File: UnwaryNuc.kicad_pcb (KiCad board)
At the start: 6 copper layers, 123.2 x 77.5 mm, 27 parts, among them Q1 2N3904, U1 NUC980DF71YC, U2 LAN8740A-EN-TR, U3 LAN8740A-EN-TR, U4 LD3985G18R_TSOT23, U5 LDK130-33_SOT23_SOT353

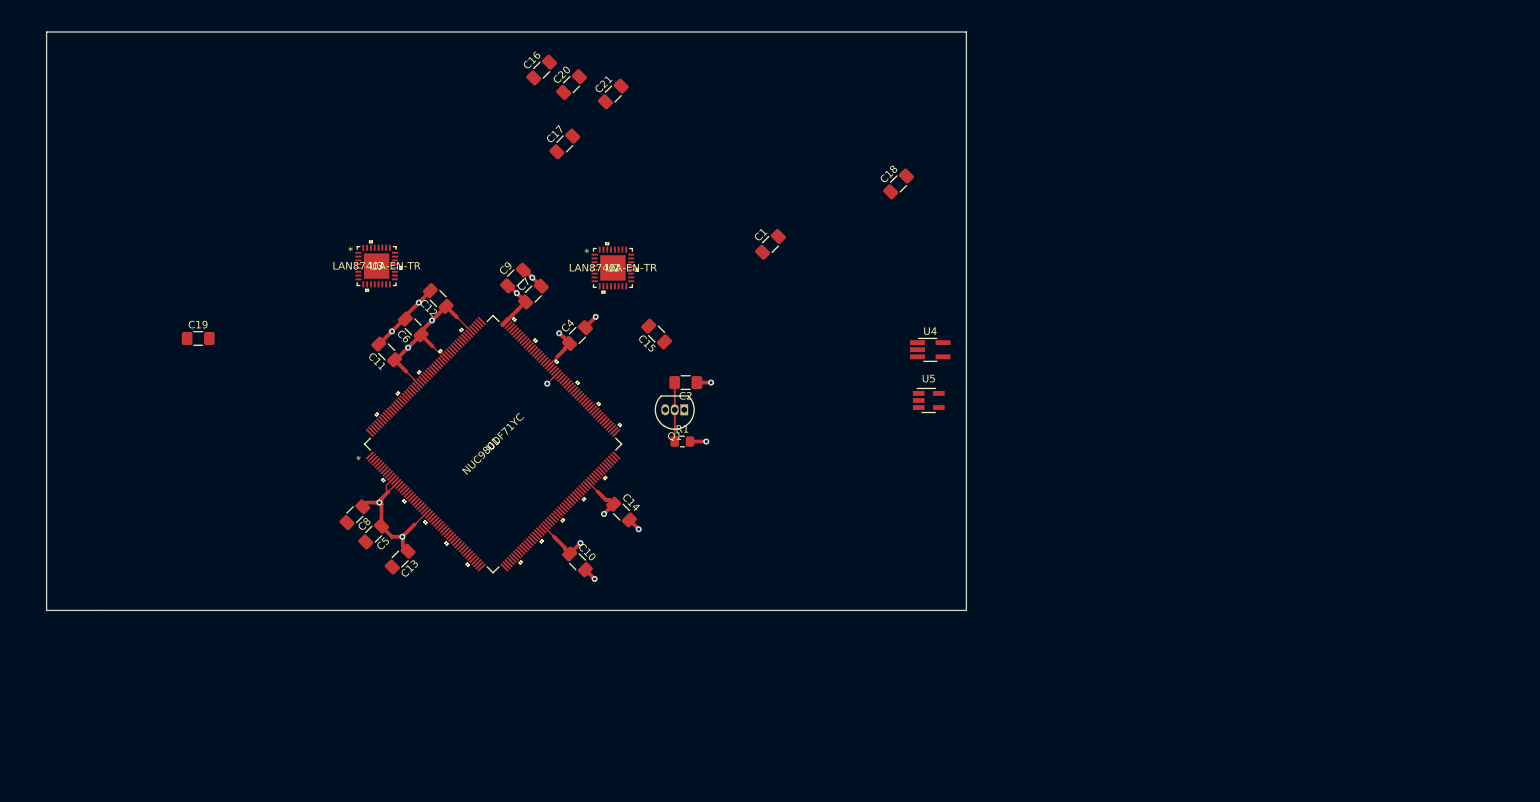
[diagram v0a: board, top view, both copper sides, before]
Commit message: added supply sequencing and stuff
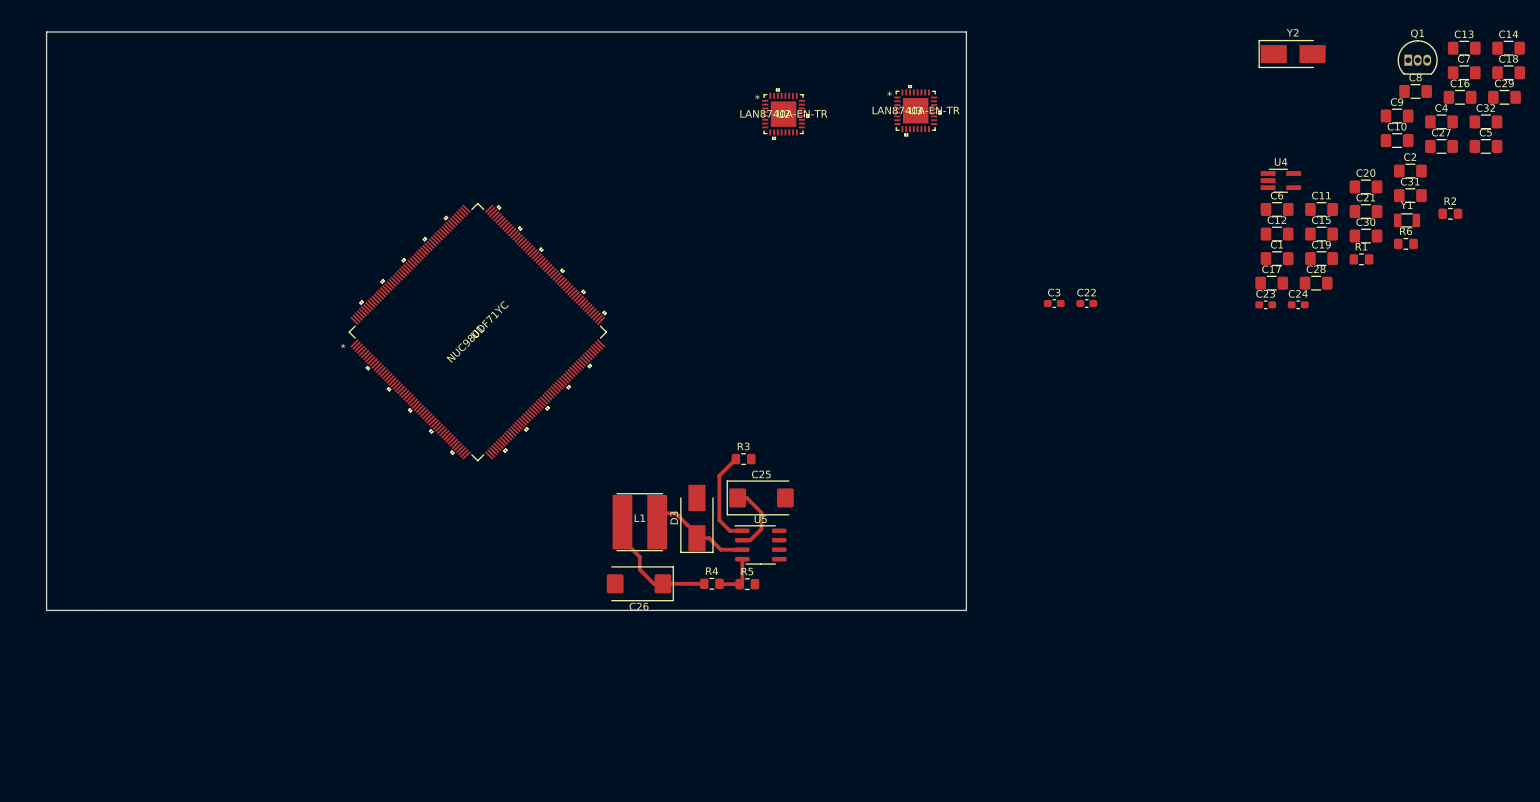
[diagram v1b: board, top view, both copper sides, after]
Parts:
- added C22: 8pf, Capacitor_SMD:C_0603_1608Metric_Pad1.05x0.95mm_HandSolder, F.Cu at (221.9, 87.2)
- added C23: 7pf, Capacitor_SMD:C_0603_1608Metric_Pad1.05x0.95mm_HandSolder, F.Cu at (245.8, 87.3)
- added C24: 7pf, Capacitor_SMD:C_0603_1608Metric_Pad1.05x0.95mm_HandSolder, F.Cu at (250.2, 87.3)
- added C25: T491D226k035AT, Capacitor_Tantalum_SMD:CP_EIA-7343-15_Kemet-W_Pad2.25x2.55mm_HandSolder, F.Cu at (178.3, 113.2)
- added C26: 293D127X96, Capacitor_Tantalum_SMD:CP_EIA-7343-43_Kemet-X_Pad2.25x2.55mm_HandSolder, F.Cu at (161.9, 124.7)
- added C27: 1u, Capacitor_SMD:C_1206_3216Metric_Pad1.42x1.75mm_HandSolder, F.Cu at (269.4, 66.1)
- added C28: 10n, Capacitor_SMD:C_1206_3216Metric_Pad1.42x1.75mm_HandSolder, F.Cu at (252.6, 84.4)
- added C29: 1u, Capacitor_SMD:C_1206_3216Metric_Pad1.42x1.75mm_HandSolder, F.Cu at (277.8, 59.5)
- added C3: 8pf, Capacitor_SMD:C_0603_1608Metric_Pad1.05x0.95mm_HandSolder, F.Cu at (217.5, 87.2)
- added C30: 1u, Capacitor_SMD:C_1206_3216Metric_Pad1.42x1.75mm_HandSolder, F.Cu at (259.2, 78.1)
- added C31: 1u, Capacitor_SMD:C_1206_3216Metric_Pad1.42x1.75mm_HandSolder, F.Cu at (265.2, 72.7)
- added C32: 1u, Capacitor_SMD:C_1206_3216Metric_Pad1.42x1.75mm_HandSolder, F.Cu at (275.3, 62.8)
- added D3: B240, 40V 2A, Diode_SMD:D_SMB_Handsoldering, F.Cu at (169.7, 115.9)
- added L1: CDRH6D38NP-150NC, UnwaryNuc:CDRH6D38_Sumida, F.Cu at (162.0, 116.5)
- added R2: 100k, Resistor_SMD:R_0805_2012Metric_Pad1.15x1.40mm_HandSolder, F.Cu at (270.6, 75.2)
- added R3: 100k, Resistor_SMD:R_0805_2012Metric_Pad1.15x1.40mm_HandSolder, F.Cu at (175.9, 108.0)
- added R4: 3.01k, Resistor_SMD:R_0805_2012Metric_Pad1.15x1.40mm_HandSolder, F.Cu at (171.7, 124.7)
- added R5: 1.78k, Resistor_SMD:R_0805_2012Metric_Pad1.15x1.40mm_HandSolder, F.Cu at (176.4, 124.8)
- added R6: 100k, Resistor_SMD:R_0805_2012Metric_Pad1.15x1.40mm_HandSolder, F.Cu at (264.6, 79.2)
- added Y1: ABS07-166, Crystal:Crystal_SMD_3215-2Pin_3.2x1.5mm, F.Cu at (264.8, 76.0)
- added Y2: NX5032GA, Crystal:Crystal_SMD_5032-2Pin_5.0x3.2mm_HandSoldering, F.Cu at (249.5, 53.8)
- U1: footprint footprints:NUC980DF71YC -> UnwaryNuc:NUC980DF71YC
- U4: value LD3985G18R_TSOT23 -> LD3985M18R_TSOT23
- U5: value LDK130-33_SOT23_SOT353 -> MIC4690; footprint Package_TO_SOT_SMD:SOT-23-5_HandSoldering -> Package_SO:SOIC-8_3.9x4.9mm_P1.27mm
- moved C13 158.1 mm to (272.4, 53.0), turned to 0 degrees
- moved C5 157.8 mm to (275.3, 66.1), turned to 0 degrees
- moved C8 153.0 mm to (265.9, 58.8), turned to 0 degrees
- moved C19 150.8 mm to (253.3, 81.2)
- moved C14 134.1 mm to (278.4, 53.0), turned to 0 degrees
- moved C7 128.1 mm to (272.4, 56.3), turned to 0 degrees
- moved C11 126.6 mm to (253.3, 74.6), turned to 0 degrees
- moved C10 123.4 mm to (263.4, 65.3), turned to 0 degrees
- moved C16 123.1 mm to (271.9, 59.5), turned to 0 degrees
- moved C9 120.0 mm to (263.4, 62.0), turned to 0 degrees
- moved C4 119.2 mm to (269.4, 62.8), turned to 0 degrees
- moved C6 116.8 mm to (247.3, 74.6), turned to 0 degrees
- moved C12 112.7 mm to (247.3, 77.9), turned to 0 degrees
- moved Q1 107.7 mm to (264.9, 54.6), turned to 0 degrees
- moved C20 107.3 mm to (259.2, 71.5), turned to 0 degrees
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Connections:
- U4 pad 2: Net-(U4-Pad2) -> GND
- U4 pad 5: Net-(U4-Pad5) -> +1V8
- U5 pad 5: Net-(U5-Pad5) -> GND
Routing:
- net +1V2: track 76.7 -> 0.00 mm, vias 9 -> 0
- net GND: track 21.1 -> 0.00 mm, vias 7 -> 0
- net /nRST: track 20.2 -> 0.00 mm, vias 1 -> 0
- net +3V3: track 0.00 -> 16.7 mm
- net Net-(R3-Pad1): track 0.00 -> 12.8 mm
- net Net-(D3-Pad1): track 0.00 -> 12.4 mm
- net Net-(C25-Pad1): track 0.00 -> 9.40 mm
- net Net-(C2-Pad2): track 7.91 -> 0.00 mm
- net Net-(R4-Pad2): track 0.00 -> 6.21 mm

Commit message: usb's connected, rmii nets assigned, some placement done
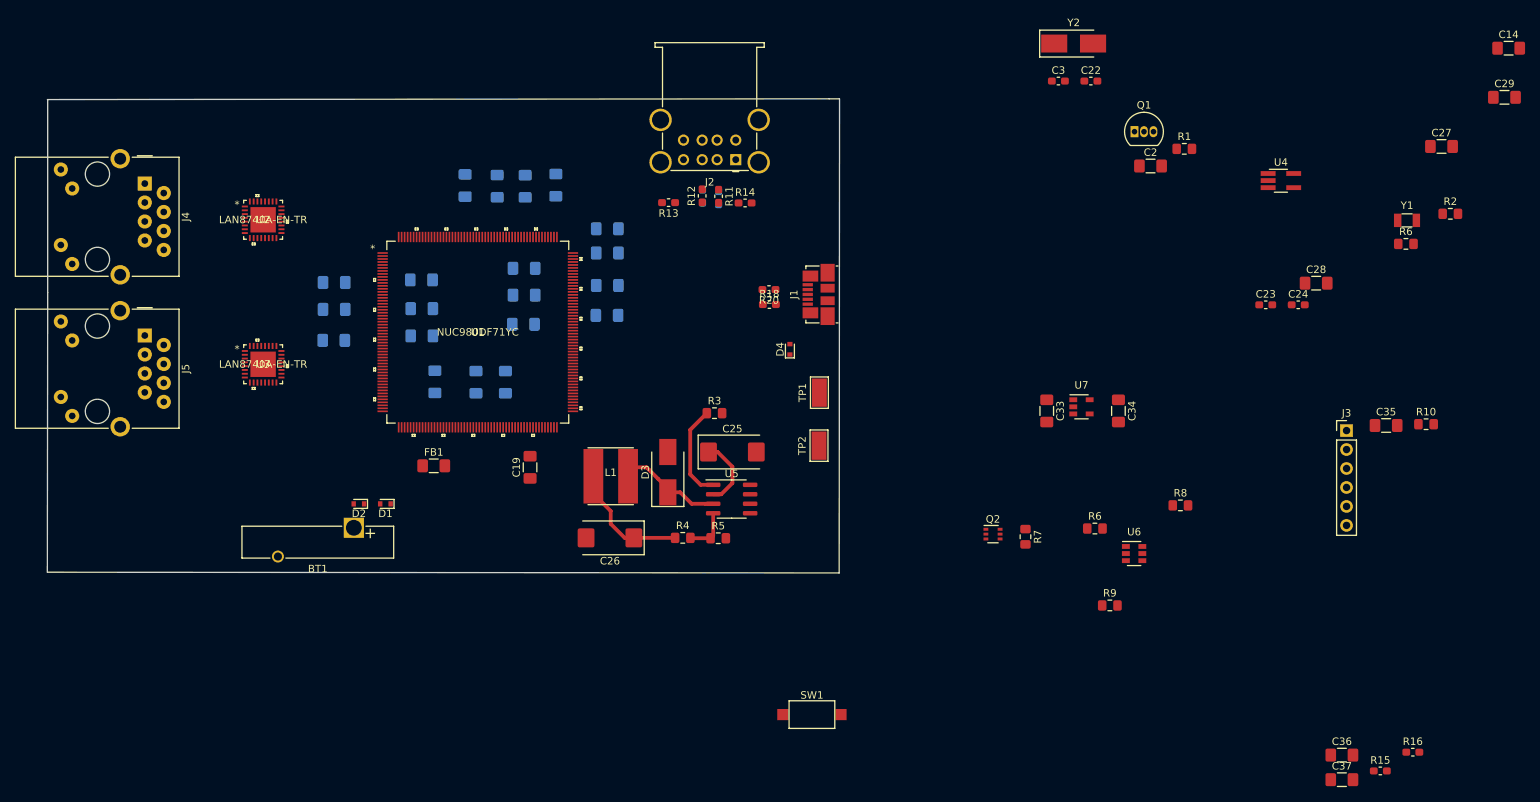
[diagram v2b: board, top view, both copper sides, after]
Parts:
- added BT1: Battery_Cell, Battery:Battery_Panasonic_CR2032-VS1N_Vertical_CircularHoles, F.Cu at (123.7, 117.2)
- added C33: 1u, Capacitor_SMD:C_1206_3216Metric_Pad1.42x1.75mm_HandSolder, F.Cu at (216.5, 101.5)
- added C34: 1u, Capacitor_SMD:C_1206_3216Metric_Pad1.42x1.75mm_HandSolder, F.Cu at (226.1, 101.5)
- added C35: 1u, Capacitor_SMD:C_1206_3216Metric_Pad1.42x1.75mm_HandSolder, F.Cu at (261.9, 103.5)
- added C36: 1u, Capacitor_SMD:C_1206_3216Metric_Pad1.42x1.75mm_HandSolder, F.Cu at (256.0, 147.6)
- added C37: 1u, Capacitor_SMD:C_1206_3216Metric_Pad1.42x1.75mm_HandSolder, F.Cu at (256.0, 150.9)
- added D1: D, Diode_SMD:D_SOD-523, F.Cu at (127.9, 114.0)
- added D2: D, Diode_SMD:D_SOD-523, F.Cu at (124.4, 114.0)
- added D4: D, Diode_SMD:D_SOD-523, F.Cu at (182.1, 93.3)
- added FB1: Ferrite_Bead_Small, Inductor_SMD:L_1206_3216Metric_Pad1.42x1.75mm_HandSolder, F.Cu at (134.4, 108.9)
- added J1: USB_B_Micro, Connector_USB:USB_Micro-B_Molex_47346-0001, F.Cu at (185.9, 86.0)
- added J2: USB_A_Dual, Connector_USB:USB_A_Wuerth_61400826021_Horizontal_Stacked, F.Cu at (174.8, 67.9)
- added J3: Conn_01x06_Male, Connector_PinHeader_2.54mm:PinHeader_1x06_P2.54mm_Vertical, F.Cu at (256.6, 104.2)
- added J4: RJ45_Amphenol_RJMG1BD3B8K1ANR, Connector_RJ:RJ45_Amphenol_RJMG1BD3B8K1ANR, F.Cu at (95.7, 71.1)
- added J5: RJ45_Amphenol_RJMG1BD3B8K1ANR, Connector_RJ:RJ45_Amphenol_RJMG1BD3B8K1ANR, F.Cu at (95.7, 91.5)
- added Q2: BC856BDW1, Package_TO_SOT_SMD:SOT-363_SC-70-6, F.Cu at (209.3, 118.0)
- added R10: 100k, Resistor_SMD:R_0805_2012Metric_Pad1.15x1.40mm_HandSolder, F.Cu at (267.3, 103.3)
- added R11: 27, Resistor_SMD:R_0603_1608Metric_Pad1.05x0.95mm_HandSolder, F.Cu at (172.6, 72.8)
- added R12: 27, Resistor_SMD:R_0603_1608Metric_Pad1.05x0.95mm_HandSolder, F.Cu at (170.3, 72.8)
- added R13: R, Resistor_SMD:R_0603_1608Metric_Pad1.05x0.95mm_HandSolder, F.Cu at (165.8, 73.7)
- added R14: R, Resistor_SMD:R_0603_1608Metric_Pad1.05x0.95mm_HandSolder, F.Cu at (176.1, 73.7)
- added R15: 12.1k, Resistor_SMD:R_0603_1608Metric_Pad1.05x0.95mm_HandSolder, F.Cu at (261.2, 149.8)
- added R16: 12.1k, Resistor_SMD:R_0603_1608Metric_Pad1.05x0.95mm_HandSolder, F.Cu at (265.5, 147.3)
- added R17: 4.7, Resistor_SMD:R_0603_1608Metric_Pad1.05x0.95mm_HandSolder, B.Cu at (170.4, 72.8)
- added R18: 4.7, Resistor_SMD:R_0603_1608Metric_Pad1.05x0.95mm_HandSolder, F.Cu at (179.3, 87.3)
- added R19: 4.7, Resistor_SMD:R_0603_1608Metric_Pad1.05x0.95mm_HandSolder, B.Cu at (172.6, 73.0)
- added R20: 4.7, Resistor_SMD:R_0603_1608Metric_Pad1.05x0.95mm_HandSolder, F.Cu at (179.3, 85.3)
- added R6: 100k, Resistor_SMD:R_0805_2012Metric_Pad1.15x1.40mm_HandSolder, F.Cu at (222.9, 117.3)
- added R7: 100k, Resistor_SMD:R_0805_2012Metric_Pad1.15x1.40mm_HandSolder, F.Cu at (213.7, 118.4)
- added R8: 100k, Resistor_SMD:R_0805_2012Metric_Pad1.15x1.40mm_HandSolder, F.Cu at (234.4, 114.2)
- added R9: 100k, Resistor_SMD:R_0805_2012Metric_Pad1.15x1.40mm_HandSolder, F.Cu at (224.9, 127.6)
- added SW1: SW_SPST, Button_Switch_SMD:SW_SPST_CK_RS282G05A3, F.Cu at (185.1, 142.2)
- added TP1: TestPoint, TestPoint:TestPoint_Keystone_5019_Minature, F.Cu at (186.1, 99.1)
- added TP2: TestPoint, TestPoint:TestPoint_Keystone_5019_Minature, F.Cu at (186.0, 106.2)
- added U6: LM3880, Package_TO_SOT_SMD:SOT-23-6, F.Cu at (228.2, 120.7)
- added U7: AP2127K-1.2, Package_TO_SOT_SMD:SOT-23-5, F.Cu at (221.2, 101.0)
- C1, C10, C11, C12, C13, C15, C16, C17, C18, C20, C21, C30, C31, C32, C4, C5, C6, C7, C8, C9: moved to B.Cu
- moved C8 148.7 mm to (121.0, 92.1), turned to 180 degrees
- moved C9 144.1 mm to (121.1, 84.3), turned to 180 degrees
- moved C5 138.9 mm to (140.1, 97.7), turned to 90 degrees
- moved C18 135.2 mm to (146.5, 86.0), turned to 180 degrees
- moved C11 132.9 mm to (121.1, 88.0), turned to 180 degrees
- moved C4 130.1 mm to (144.0, 97.7), turned to 90 degrees
- moved C20 128.0 mm to (132.8, 91.5)
- moved C16 127.4 mm to (146.5, 82.5), turned to 180 degrees
- moved C7 122.6 mm to (150.8, 71.3), turned to 90 degrees
- moved C15 120.9 mm to (132.8, 87.8)
- moved C32 120.5 mm to (157.6, 88.8)
- moved C13 119.1 mm to (157.7, 84.8)
- moved C10 116.9 mm to (146.7, 71.5), turned to 90 degrees
- moved C1 114.0 mm to (134.6, 97.7), turned to 90 degrees
- moved C17 113.9 mm to (132.8, 84.0)
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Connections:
- net Net-(C25-Pad1) renamed +5V
- net Net-(R3-Pad1) renamed /3V3EN
- net Net-(U1-Pad153) renamed /RMII1_RXERR
- net Net-(U1-Pad154) renamed /RMII1_CRSDV
- net Net-(U1-Pad155) renamed /RMII1_RXD1
- net Net-(U1-Pad156) renamed /RMII1_RXD0
- net Net-(U1-Pad157) renamed /RMII1_REFCLK
- net Net-(U1-Pad158) renamed /RMII1_TXEN
- net Net-(U1-Pad159) renamed /RMII1_TXD1
- net Net-(U1-Pad165) renamed /RMII1_TXD0
- net Net-(U1-Pad166) renamed /RMII1_MDIO
- net Net-(U1-Pad167) renamed /RMII1_MDC
- net Net-(U1-Pad177) renamed /RMII0_RXERR
- net Net-(U1-Pad178) renamed /RMII0_CRSDV
- net Net-(U1-Pad179) renamed /RMII0_RXD1
- net Net-(U1-Pad181) renamed /RMII0_RXD0
- net Net-(U1-Pad182) renamed /RMII0_REFCLK
- net Net-(U1-Pad183) renamed /RMII0_TXEN
- net Net-(U1-Pad184) renamed /RMII0_TXD1
- net Net-(U1-Pad185) renamed /RMII0_TXD0
- net Net-(U1-Pad187) renamed /RMII0_MDIO
- net Net-(U1-Pad188) renamed /RMII0_MDC
- net Net-(U1-Pad190) renamed /USB0_VBUSVLD
- C27 pad 1: Net-(C27-Pad1) -> +3V3
- U1 pad 130: Net-(U1-Pad130) -> /USBHL.DD_N
- U1 pad 131: Net-(U1-Pad131) -> /USBHL.DD_P
- U1 pad 170: Net-(U1-Pad170) -> /UART0_RXD
- U1 pad 172: Net-(U1-Pad172) -> /UART0_TXD
- U1 pad 195: Net-(U1-Pad195) -> +1V2
- U1 pad 196: Net-(U1-Pad196) -> +1V2
- U1 pad 197: Net-(U1-Pad197) -> GND
- U1 pad 200: Net-(U1-Pad200) -> GND
- U1 pad 203: Net-(U1-Pad203) -> +3V3
- U1 pad 204: Net-(U1-Pad204) -> +3V3
- U1 pad 206: Net-(U1-Pad206) -> +1V2
- U1 pad 207: Net-(U1-Pad207) -> +1V2
- U1 pad 208: Net-(U1-Pad208) -> GND
- U1 pad 211: Net-(U1-Pad211) -> GND
- U1 pad 212: Net-(U1-Pad212) -> /USB0.DD_N
- U1 pad 213: Net-(U1-Pad213) -> /USB0.DD_P
- U1 pad 214: Net-(U1-Pad214) -> +3V3
- U1 pad 215: Net-(U1-Pad215) -> +3V3
- U4 pad 1: Net-(C27-Pad1) -> +3V3
- U4 pad 3: Net-(R6-Pad1) -> /1V8_EN
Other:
- board size 123.2 x 77.5 mm -> 106.1 x 63.5 mm
